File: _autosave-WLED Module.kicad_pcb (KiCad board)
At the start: 2 copper layers, 86.9 x 46.7 mm, 21 parts, among them IC1 SN74AHCT125D, J1 Conn_02x03_Odd_Even, J2 JST SM Connector, J3 Conn_01x02_Male, J4 Conn_01x02_Male, U1 ESP32-WROOM-32D, U2 AMS1117-3.3

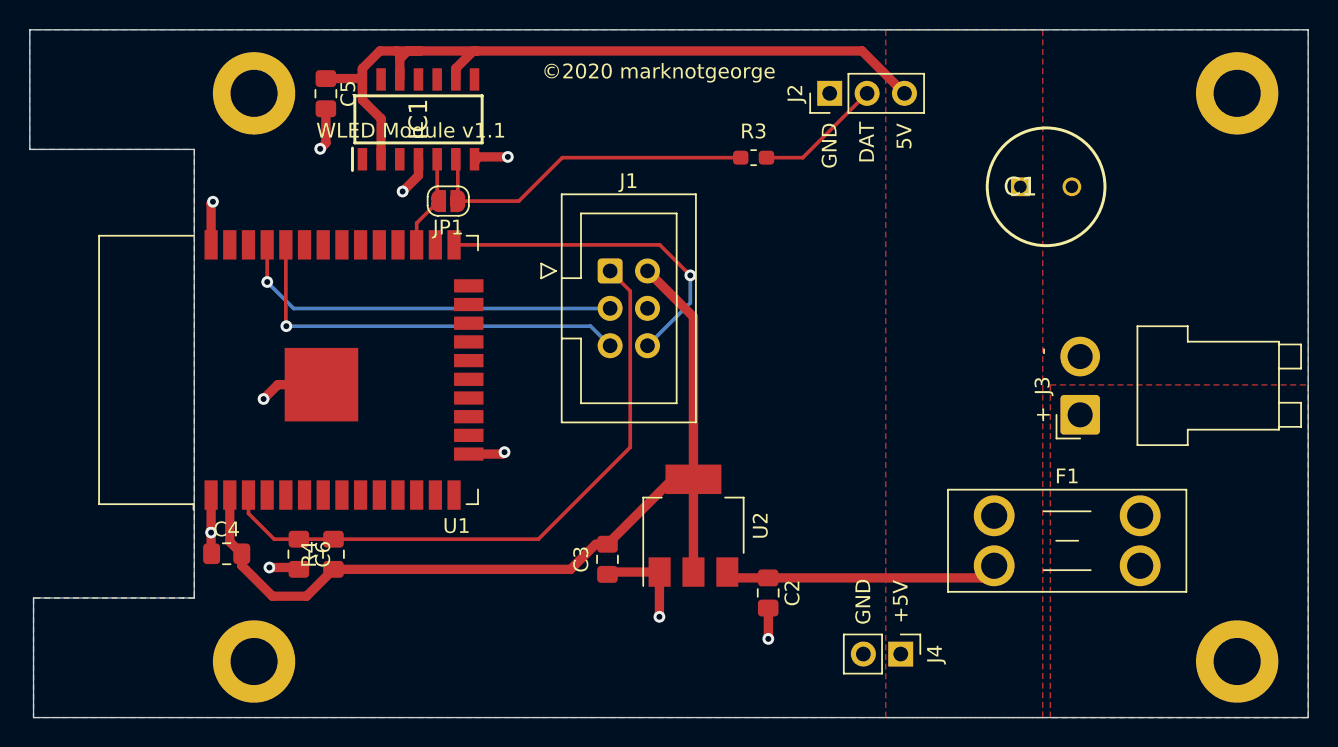
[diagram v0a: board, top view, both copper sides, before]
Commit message: V1.2
* Auto-save circuitry replaced in favour of ESP-Prog interface.
* Ancillary components rearranged.
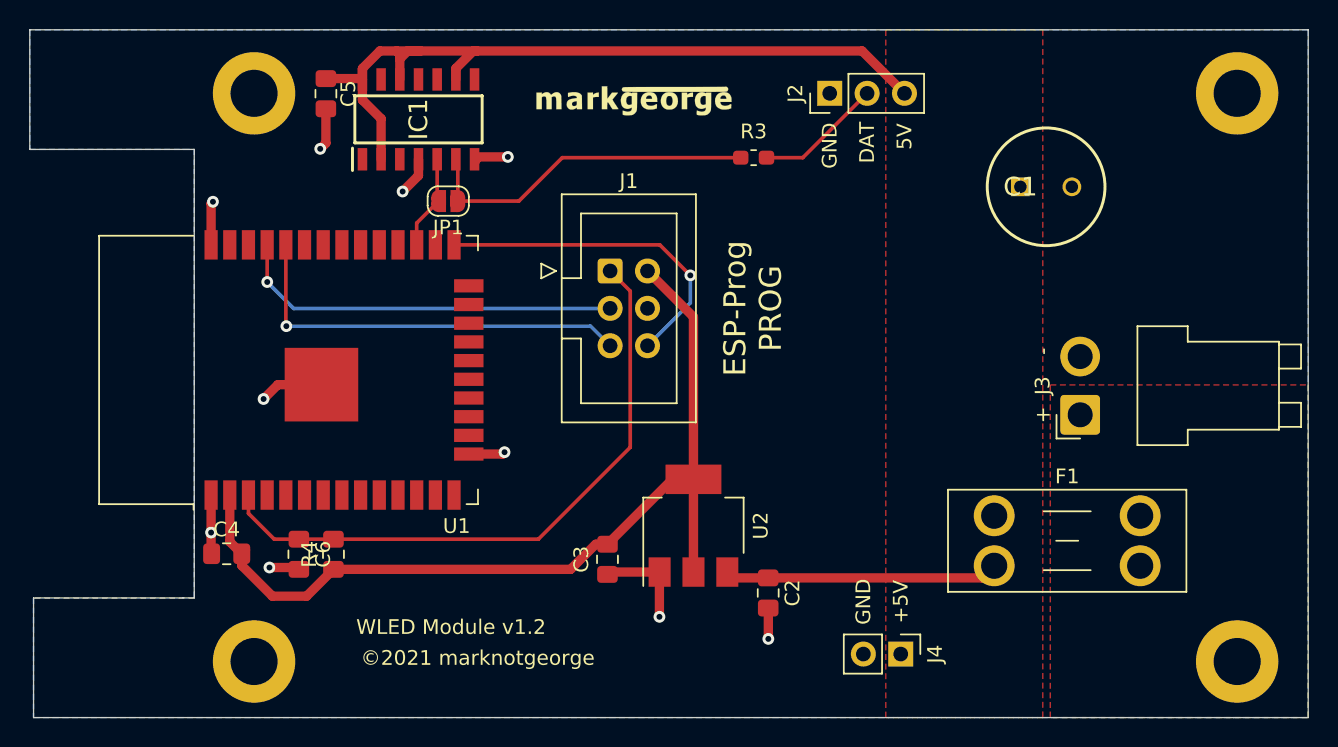
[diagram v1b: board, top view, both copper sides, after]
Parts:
- added G***: LOGO, WLED Module:marknotgeorge logo, F.Cu at (213.4, 88.2)
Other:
- board text added: "ESP-Prog PROG"
- board text added: "WLED Module v1.2"
- board text added: "©2021 marknotgeorge"
- board text removed: "WLED Module v1.1"
- board text removed: "©2020 marknotgeorge"
